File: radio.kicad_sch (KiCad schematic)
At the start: 34 parts, among them Q1 BSS138W-7-F, U2 SX1276, X1 AS183-92LF, Y1 ECS-TXO-25CSMV-320-AM-TR

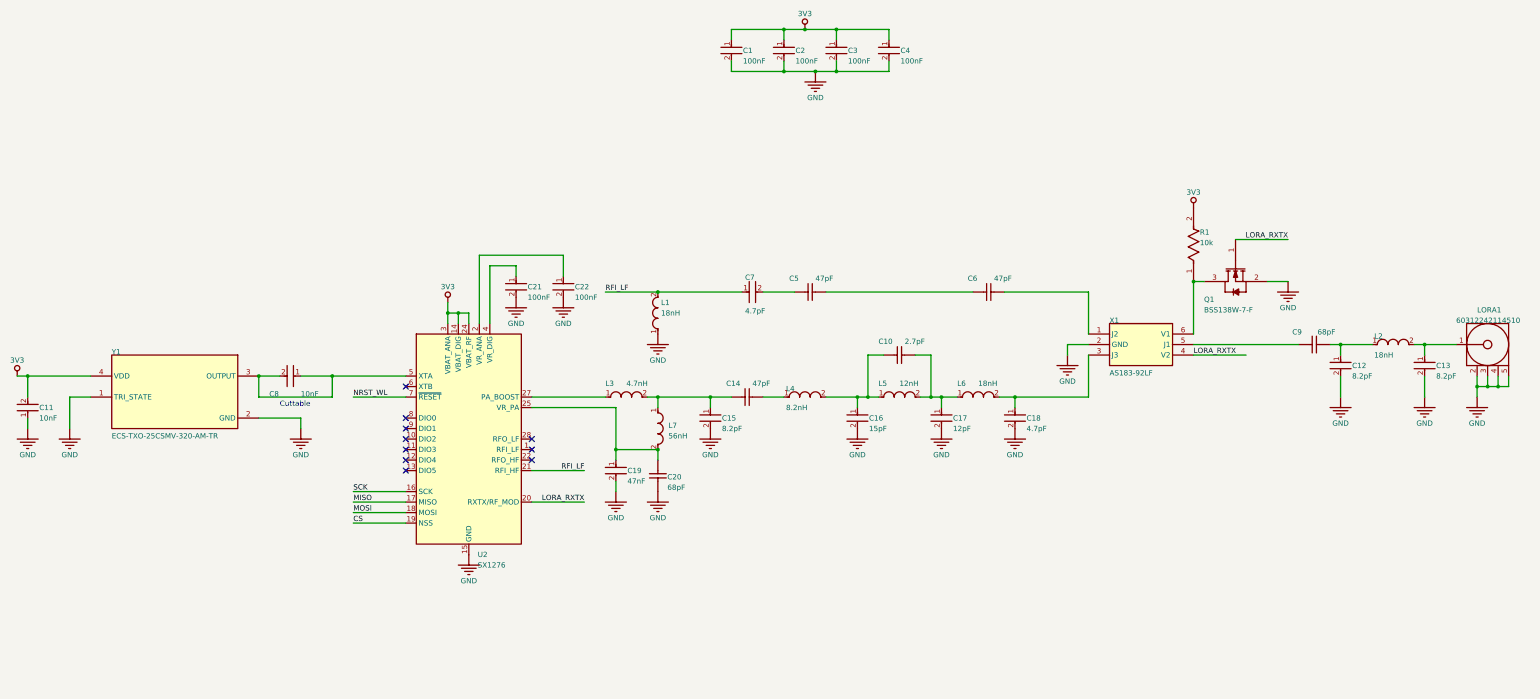
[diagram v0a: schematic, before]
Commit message: added radio receiver control
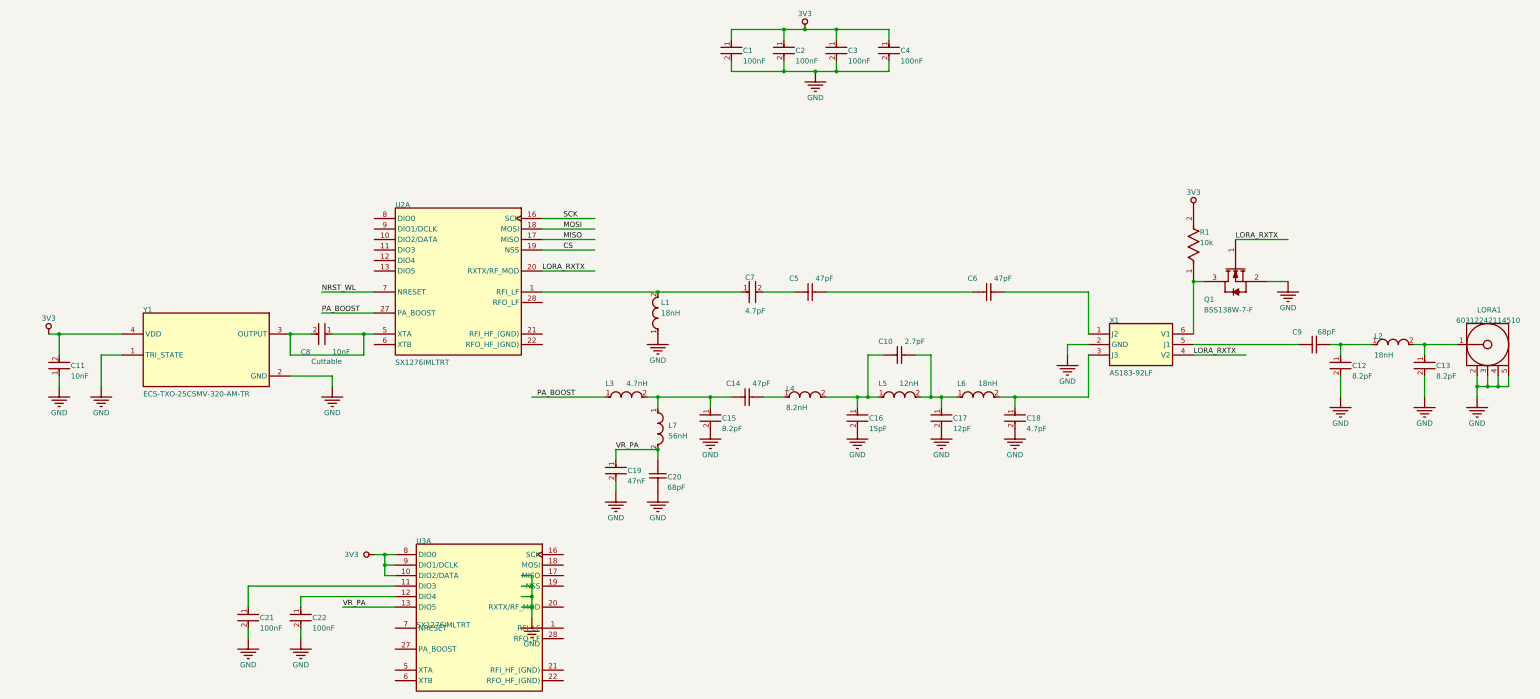
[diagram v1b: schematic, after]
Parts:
- removed U2: SX1276, Package_DFN_QFN:QFN-28-1EP_6x6mm_P0.65mm_EP4.8x4.8mm, symbol RF:SX1276
- added C21: 100nF, FP-C0603C-CF-MFG, symbol Altium Content Vault:root_0_b4654b650e69147ec39a6b967a45e02_Altium Content Vault
- added U2, U3: SX1276IMLTRT, SMTC-QFN-28_V, symbol Altium Content Vault:root_0_SMTC-SX127X-QFN-28_Altium Content Vault
- renumbered C21 to C1
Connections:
- net 3V3: now also U3.10 (DIO2/DATA), U3.8 (DIO0), U3.9 (DIO1/DCLK)
- net CS: now also U2.19 (NSS)
- net GND: now also C21.2
- net LORA_RXTX: now also U2.20 (RXTX/RF_MOD)
- net MISO: now also U2.17 (MISO)
- net MOSI: now also U2.18 (MOSI)
- net NRST_WL: now also U2.7 (NRESET)
- net SCK: now also U2.16 (SCK)
- net VR_PA: now reaches C19.1, C20.2, L7.2
- net VR_PA: now also U3.13 (DIO5)
- net at C22.1: now also U3.12 (DIO4)
- net at C8.1, C8.2, Y1.3 (OUTPUT): now also U2.5 (XTA)
- net PA_BOOST: now reaches L3.1
- net PA_BOOST: now also U2.27 (PA_BOOST)
- net RFI_LF: no longer names the net of C7.1, L1.2
- net RFI_LF: now also U2.1 (RFI_LF)
- new net: C21.1, U3.11 (DIO3)
- no-connect marks 10 -> 0
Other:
- moved on the sheet: C11, C8, Y1

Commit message: fix sx1276
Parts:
- removed C21: 100nF, FP-C0603C-CF-MFG, symbol Altium Content Vault:root_0_b4654b650e69147ec39a6b967a45e02_Altium Content Vault
- removed U2, U3: SX1276IMLTRT, SMTC-QFN-28_V, symbol Altium Content Vault:root_0_SMTC-SX127X-QFN-28_Altium Content Vault
- added U2: SX1276, Package_DFN_QFN:QFN-28-1EP_6x6mm_P0.65mm_EP4.8x4.8mm, symbol RF:SX1276
- renumbered C1 to C21
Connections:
- net 3V3: now also U2.14 (VBAT_DIG), U2.24 (VBAT_RF), U2.3 (VBAT_ANA)
- net CS: now also U2.19 (NSS)
- net GND: now also U2.15 (GND), U2.23 (GND), U2.26 (GND), U2.29 (GND)
- net LORA_RXTX: now also U2.20 (RXTX/RF_MOD)
- net MISO: now also U2.17 (MISO)
- net MOSI: now also U2.18 (MOSI)
- net NRST_WL: now also U2.7 (~{RESET})
- net SCK: now also U2.16 (SCK)
- net at C22.1: now also U2.2 (VR_ANA)
- net RFI_LF: now reaches C7.1, L1.2
- net RFI_LF: now also U2.21 (RFI_HF)
- net at C8.1, C8.2, Y1.3 (OUTPUT): now also U2.5 (XTA)
- net PA_BOOST: no longer names the net of L3.1
- net PA_BOOST: now also U2.27 (PA_BOOST)
- net VR_PA: no longer names the net of C19.1, C20.2, L7.2
- net VR_PA: now also U2.25 (VR_PA)
- new net: C21.1, U2.4 (VR_DIG)
- no-connect marks 0 -> 10
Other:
- moved on the sheet: C11, C8, Y1
